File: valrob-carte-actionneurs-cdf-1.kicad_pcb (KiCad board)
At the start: 4 copper layers, 50 x 50 mm, 126 parts, among them J1 USB_C_Receptacle_USB2.0_14P, J2 Conn_01x02, J3 Conn_01x02, J4 Conn_01x04_Pin, J5 Conn_01x02, J6 Conn_01x02, J7 Conn_01x12, M1 Motor_Servo, M10 Motor_Servo, M11 Motor_Servo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

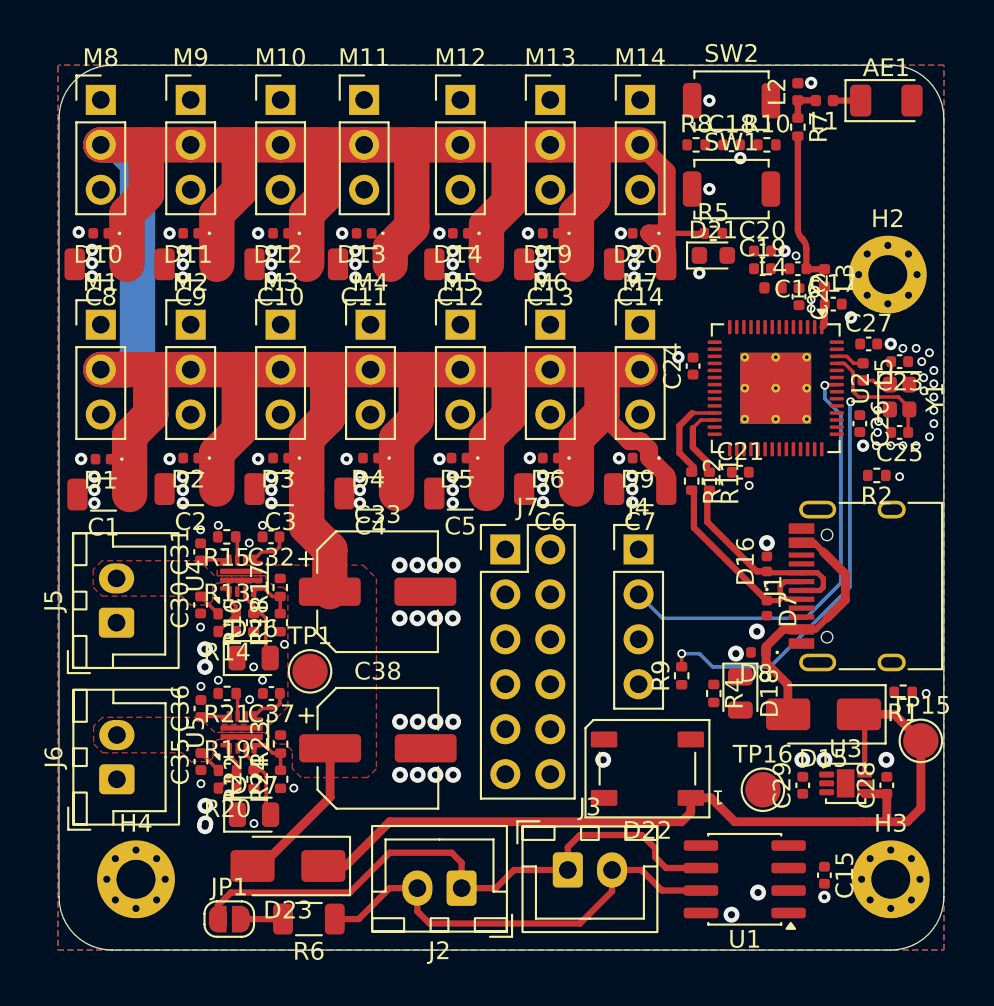
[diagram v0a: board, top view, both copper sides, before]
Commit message: pcb: add servo PWM routing
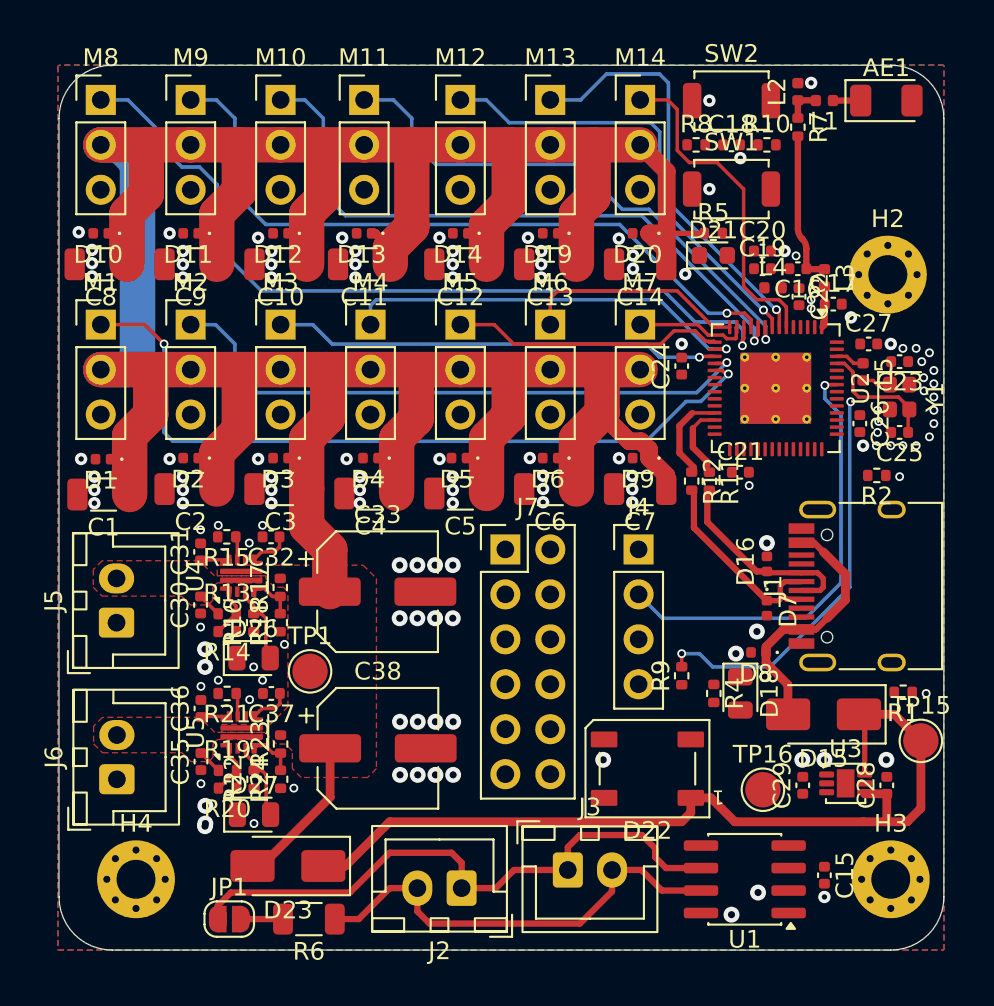
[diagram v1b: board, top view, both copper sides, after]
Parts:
- moved C24 0.64 mm to (119.2, 76.0)
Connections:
- U2 pad 13: /SERVO6 -> /SERVO7
- U2 pad 14: /SERVO7 -> /SERVO6
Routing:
- net /SERVO8: track 0.00 -> 46.2 mm, vias 0 -> 1
- net /SERVO1: track 0.00 -> 43.6 mm, vias 0 -> 2
- net /SERVO9: track 0.00 -> 39.7 mm, vias 0 -> 1
- net /SERVO10: track 0.00 -> 36.2 mm, vias 0 -> 1
- net /SERVO2: track 0.00 -> 34.2 mm, vias 0 -> 1
- net /SERVO11: track 0.00 -> 30.2 mm, vias 0 -> 1
- net /SERVO12: track 0.00 -> 25.7 mm, vias 0 -> 1
- net /SERVO3: track 0.00 -> 25.3 mm, vias 0 -> 1
- net /SERVO13: track 0.00 -> 23.9 mm, vias 0 -> 1
- net /SERVO4: track 0.00 -> 23.1 mm, vias 0 -> 1
- net /SERVO14: track 0.00 -> 18.8 mm
- net /SERVO5: track 0.00 -> 15.4 mm
- net /SERVO6: track 0.00 -> 12.7 mm
- net /SERVO7: track 0.00 -> 6.40 mm
- net +5V: track 197.8 -> 199.2 mm
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
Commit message: pcb: add usb c routing
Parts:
- moved R1 9.88 mm to (122.4, 91.0), turned to 0 degrees
- moved R2 6.29 mm to (124.2, 84.0), turned to -90 degrees
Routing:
- net Net-(J1-CC1): track 0.00 -> 3.80 mm
- net Net-(J1-CC2): track 0.00 -> 3.40 mm

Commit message: pcb: add BOOT and CHIP_PU routing
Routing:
- net /CHIP_PU: track 0.00 -> 20.9 mm, vias 0 -> 2
- net /BOOT: track 0.00 -> 13.2 mm, vias 0 -> 2
- net Net-(D21-A): track 0.00 -> 1.36 mm
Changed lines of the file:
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@@
 	)
 	(segment
+		(start 125.9 74.690951)
+		(end 125.804932 74.786019)
+		(width 0.2)
+		(layer "F.Cu")
+		(net 6)
+	)
+	(segment
+		(start 122.685 61)
+		(end 124.225 61)
+		(width 0.2)
+		(layer "F.Cu")
+		(net 6)
+	)
+	(segment
+		(start 121.52 62.165)
+		(end 122.685 61)
+		(width 0.2)
+		(layer "F.Cu")
+		(net 6)
+	)
+	(segment
+		(start 121.52 63.5)
+		(end 120.51 63.5)
+		(width 0.2)
+		(layer "F.Cu")
+		(net 6)
+	)
+	(segment
+		(start 125.9 73.8)
+		(end 125.9 74.690951)
+		(width 0.2)
+		(layer "F.Cu")
+		(net 6)
+	)
+	(segment
+		(start 121.52 63.5)
+		(end 121.52 62.165)
+		(width 0.2)
+		(layer "F.Cu")
+		(net 6)
+	)
+	(via
+		(at 121.435 62.25)
+		(size 0.5)
+		(drill 0.3)
+		(layers "F.Cu" "B.Cu")
+		(net 6)
+	)
+	(via
+		(at 125.804932 74.786019)
+		(size 0.5)
+		(drill 0.3)
+		(layers "F.Cu" "B.Cu")
+		(net 6)
+	)
+	(segment
+		(start 124.185 69.75)
+		(end 124.185 69)
+		(width 0.2)
+		(layer "B.Cu")
+		(net 6)
+	)
+	(segment
+		(start 125.804932 71.369932)
+		(end 125.185 70.75)
+		(width 0.2)
+		(layer "B.Cu")
+		(net 6)
+	)
+	(segment
+		(start 122.435 65.5)
+		(end 121.435 64.5)
+		(width 0.2)
+		(layer "B.Cu")
+		(net 6)
+	)
+	(segment
+		(start 125.185 70.75)
+		(end 124.185 69.75)
+		(width 0.2)
+		(layer "B.Cu")
+		(net 6)
+	)
+	(segment
+		(start 121.435 64.5)
+		(end 121.435 62.25)
+		(width 0.2)
+		(layer "B.Cu")
+		(net 6)
+	)
+	(segment
+		(start 124.185 69)
+		(end 124.185 67.25)
+		(width 0.2)
+		(layer "B.Cu")
+		(net 6)
+	)
+	(segment
+		(start 124.185 67.25)
+		(end 122.435 65.5)
+		(width 0.2)
+		(layer "B.Cu")
+		(net 6)
+	)
+	(segment
+		(start 125.804932 74.786019)
+		(end 125.804932 71.369932)
+		(width 0.2)
+		(layer "B.Cu")
+		(net 6)
+	)
+	(segment
 		(start 130.235 77.05)
 		(end 130.95 77.05)
@@
 	)
 	(segment
+		(start 121.4825 69.4725)
+		(end 121.76 69.75)
+		(width 0.3)
+		(layer "F.Cu")
+		(net 22)
+	)
+	(segment
+		(start 121.4825 68.5)
+		(end 121.4825 69.4725)
+		(width 0.3)
+		(layer "F.Cu")
+		(net 22)
+	)
+	(segment
 		(start 94.525 89.09)
 		(end 94.525 88.75)
@@
 	)
 	(segment
-		(start 125.115 86.68)
-		(end 124.935 86.5)
+		(start 124.935 86.5)
+		(end 124.935 85.75)
 		(width 0.2)
 		(layer "F.Cu")
@@
 	)
 	(segment
-		(start 124.185 85)
-		(end 124.185 84.51)
+		(start 125.115 86.68)
+		(end 124.935 86.5)
 		(width 0.2)
 		(layer "F.Cu")
@@
 	)
 	(segment
-		(start 124.935 86.5)
-		(end 124.935 85.75)
+		(start 124.935 85.75)
+		(end 124.185 85)
 		(width 0.2)
 		(layer "F.Cu")
@@
 	)
 	(segment
-		(start 124.935 85.75)
-		(end 124.185 85)
+		(start 124.185 85)
+		(end 124.185 84.51)
 		(width 0.2)
 		(layer "F.Cu")
@@
 	)
 	(segment
+		(start 124.185 67.5)
+		(end 124.185 66.04)
+		(width 0.2)
+		(layer "F.Cu")
+		(net 51)
+	)
+	(segment
+		(start 123.49 64.055)
+		(end 123.49 63.5)
+		(width 0.2)
+		(layer "F.Cu")
+		(net 51)
+	)
+	(segment
+		(start 123.685 68)
+		(end 124.185 67.5)
+		(width 0.2)
+		(layer "F.Cu")
+		(net 51)
+	)
+	(segment
+		(start 124.225 66)
+		(end 124.225 64.79)
+		(width 0.2)
+		(layer "F.Cu")
+		(net 51)
+	)
+	(segment
+		(start 124.185 66.04)
+		(end 124.225 66)
+		(width 0.2)
+		(layer "F.Cu")
+		(net 51)
+	)
+	(segment
+		(start 125.5 74.281454)
+		(end 125.182398 74.599056)
+		(width 0.2)
+		(layer "F.Cu")
+		(net 51)
+	)
+	(segment
+		(start 125.5 73.8)
+		(end 125.5 74.281454)
+		(width 0.2)
+		(layer "F.Cu")
+		(net 51)
+	)
+	(segment
+		(start 124.225 64.79)
+		(end 123.49 64.055)
+		(width 0.2)
+		(layer "F.Cu")
+		(net 51)
+	)
+	(via
+		(at 123.685 68)
+		(size 0.5)
+		(drill 0.3)
+		(layers "F.Cu" "B.Cu")
+		(net 51)
+	)
+	(via
+		(at 125.182398 74.599056)
+		(size 0.5)
+		(drill 0.3)
+		(layers "F.Cu" "B.Cu")
+		(net 51)
+	)
+	(segment
+		(start 123.685 70.125)
+		(end 125.182398 71.622398)
+		(width 0.2)
+		(layer "B.Cu")
+		(net 51)
+	)
+	(segment
+		(start 123.685 68)
+		(end 123.685 70.125)
+		(width 0.2)
+		(layer "B.Cu")
+		(net 51)
+	)
+	(segment
+		(start 125.182398 71.622398)
+		(end 125.182398 74.599056)
+		(width 0.2)
+		(layer "B.Cu")
+		(net 51)
+	)
+	(segment
 		(start 121.05 79.05)
 		(end 120.2645 79.05)
@@
 	)
 	(zone
-		(net 73)
-		(net_name "+5V")
-		(layer "F.Cu")
-		(name "$teardrop_track$")
-		(hatch none 0.1)
-		(priority 30002)
-		(attr
-			(teardrop
-				(type track_end)
-			)
-		)
-		(connect_pads yes
-			(clearance 0)
-		)
-		(min_thickness 0.0254)
-		(filled_areas_thickness no)
-		(fill yes
-			(thermal_gap 0.5)
-			(thermal_bridge_width 0.5)
-			(island_removal_mode 1)
-			(island_area_min 10)
-		)
-		(polygon
-			(pts
-				(xy 119.331393 68.65) (xy 119.331393 68.35) (xy 118.438545 68.009607) (xy 118.34 68.5) (xy 118.438545 68.990393)
-			)
-		)
-	)
-	(zone
 		(net 12)
 		(net_name "Net-(J5-Pin_2)")
@@
 	)
 	(zone
-		(net 73)
-		(net_name "+5V")
+		(net 52)
+		(net_name "/ESP_D+")
 		(layer "F.Cu")
 		(name "$teardrop_track$")
 		(hatch none 0.1)
-		(priority 30003)
+		(priority 30007)
 		(attr
 			(teardrop
@@
 		(polygon
 			(pts
-				(xy 119.331393 68.65) (xy 119.331393 68.35) (xy 118.438545 68.009607) (xy 118.34 68.5) (xy 118.438545 68.990393)
+				(xy 120.136623 79.319299) (xy 119.995201 79.177877) (xy 119.714775 79.350751) (xy 119.813793 79.500707)
+				(xy 119.963749 79.599725)
 			)
 		)
@@
 		(name "$teardrop_track$")
 		(hatch none 0.1)
-		(priority 30004)
+		(priority 30002)
 		(attr
 			(teardrop
@@
 	)
 	(zone
-		(net 53)
-		(net_name "/ESP_D-")
+		(net 19)
+		(net_name "+Vbus")
 		(layer "F.Cu")
 		(name "$teardrop_track$")
 		(hatch none 0.1)
-		(priority 30008)
+		(priority 30005)
 		(attr
 			(teardrop
@@
 		(polygon
 			(pts
-				(xy 120.140551 78.75) (xy 120.140551 78.55) (xy 119.820019 78.473949) (xy 119.784 78.65) (xy 119.820019 78.826051)
+				(xy 126.92448 90.473231) (xy 127.178331 90.727082) (xy 127.540455 90.457867) (xy 127.402269 90.249293)
+				(xy 127.193695 90.111107)
 			)
 		)
 	)
 	(zone
-		(net 52)
-		(net_name "/ESP_D+")
+		(net 19)
+		(net_name "+Vbus")
 		(layer "F.Cu")
 		(name "$teardrop_track$")
 		(hatch none 0.1)
-		(priority 30007)
+		(priority 30006)
 		(attr
 			(teardrop
@@
 		(polygon
 			(pts
-				(xy 120.136623 79.319299) (xy 119.995201 79.177877) (xy 119.714775 79.350751) (xy 119.813793 79.500707)
-				(xy 119.963749 79.599725)
+				(xy 126.961769 86.022918) (xy 126.707918 86.276769) (xy 126.977133 86.638893) (xy 127.185707 86.500707)
+				(xy 127.323893 86.292133)
 			)
 		)
 	)
 	(zone
-		(net 19)
-		(net_name "+Vbus")
+		(net 53)
+		(net_name "/ESP_D-")
 		(layer "F.Cu")
 		(name "$teardrop_track$")
 		(hatch none 0.1)
-		(priority 30005)
+		(priority 30008)
 		(attr
 			(teardrop
@@
 		(polygon
 			(pts
-				(xy 126.92448 90.473231) (xy 127.178331 90.727082) (xy 127.540455 90.457867) (xy 127.402269 90.249293)
-				(xy 127.193695 90.111107)
+				(xy 120.140551 78.75) (xy 120.140551 78.55) (xy 119.820019 78.473949) (xy 119.784 78.65) (xy 119.820019 78.826051)
 			)
 		)
@@
 	)
 	(zone
-		(net 19)
-		(net_name "+Vbus")
+		(net 73)
+		(net_name "+5V")
 		(layer "F.Cu")
 		(name "$teardrop_track$")
 		(hatch none 0.1)
-		(priority 30006)
+		(priority 30003)
 		(attr
 			(teardrop
@@
 		(polygon
 			(pts
-				(xy 126.961769 86.022918) (xy 126.707918 86.276769) (xy 126.977133 86.638893) (xy 127.185707 86.500707)
-				(xy 127.323893 86.292133)
+				(xy 119.331393 68.65) (xy 119.331393 68.35) (xy 118.438545 68.009607) (xy 118.34 68.5) (xy 118.438545 68.990393)
+			)
+		)
+	)
+	(zone
+		(net 73)
+		(net_name "+5V")
+		(layer "F.Cu")
+		(name "$teardrop_track$")
+		(hatch none 0.1)
+		(priority 30004)
+		(attr
+			(teardrop
+				(type track_end)
+			)
+		)
+		(connect_pads yes
+			(clearance 0)
+		)
+		(min_thickness 0.0254)
+		(filled_areas_thickness no)
+		(fill yes
+			(thermal_gap 0.5)
+			(thermal_bridge_width 0.5)
+			(island_removal_mode 1)
+			(island_area_min 10)
+		)
+		(polygon
+			(pts
+				(xy 119.331393 68.65) (xy 119.331393 68.35) (xy 118.438545 68.009607) (xy 118.34 68.5) (xy 118.438545 68.990393)
 			)
 		)

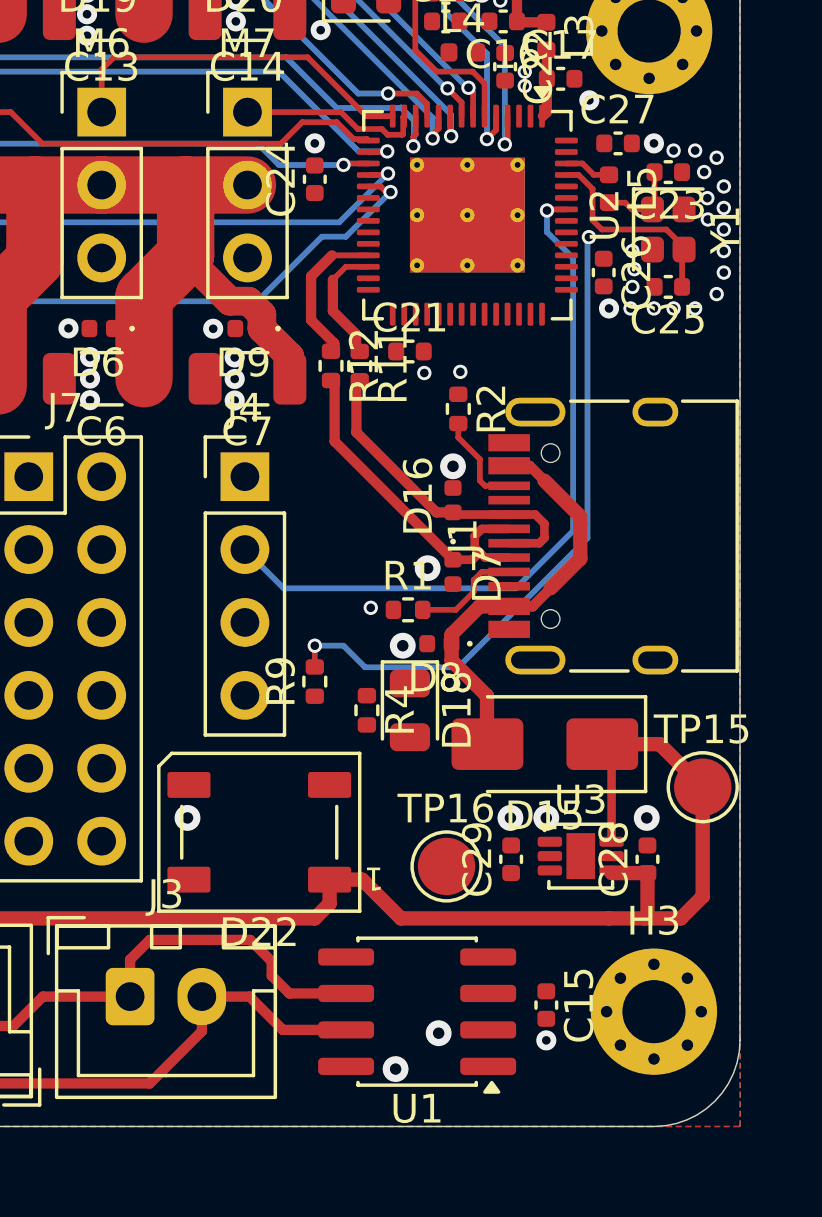
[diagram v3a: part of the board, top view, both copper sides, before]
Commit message: pcb: add CAN routing
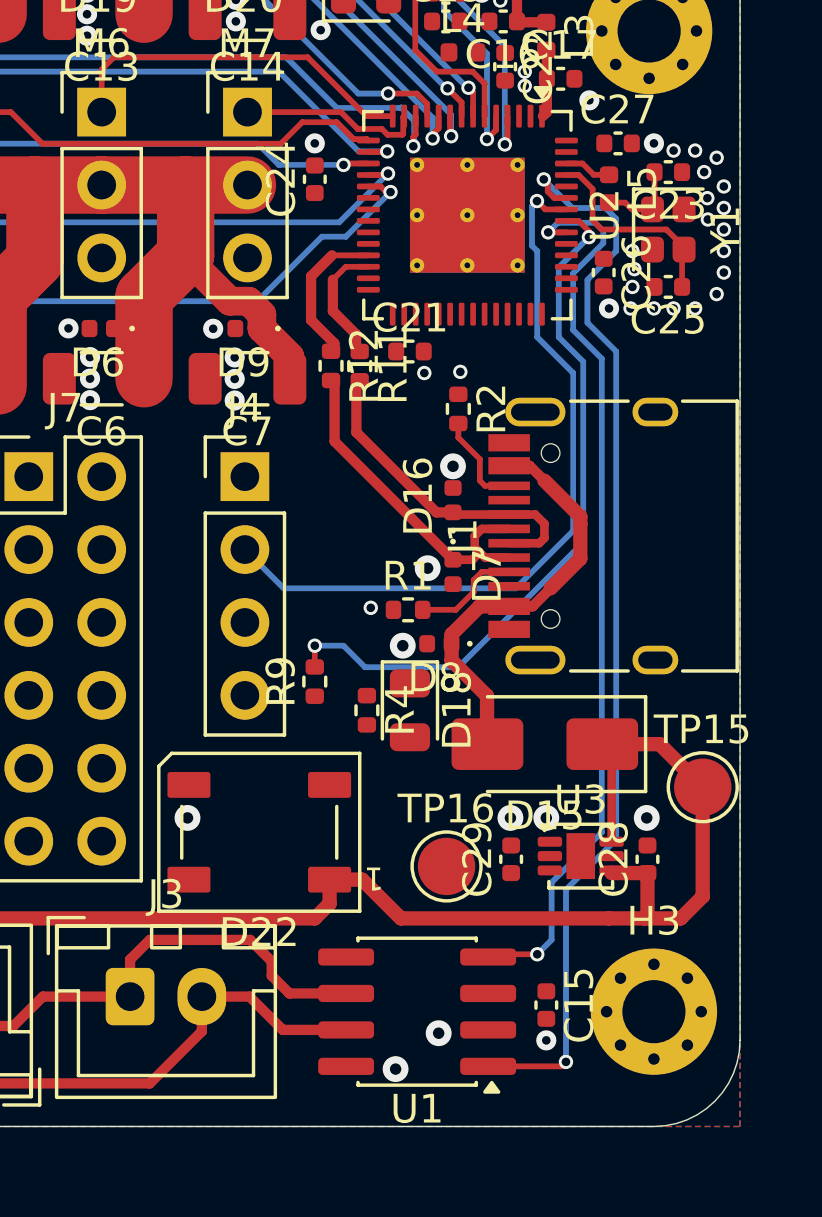
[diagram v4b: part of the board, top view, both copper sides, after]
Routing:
- net /CAN_TX: track 0.00 -> 38.0 mm, vias 0 -> 2
- net /CAN_RX: track 0.00 -> 31.5 mm, vias 0 -> 2
- net /U0TXD: track 22.9 -> 24.8 mm
- net /U0RXD: track 25.1 -> 26.1 mm
